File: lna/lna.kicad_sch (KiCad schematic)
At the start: 12 parts, among them J1 Conn_Coaxial, J2 V5-GND, U1 PGA-103+

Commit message: Schematics
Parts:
- removed C3: 0.01uF, symbol Device:C
- added C?: 0.33uF, symbol Device:C
- added C?: 10uF, symbol Device:CP1
- added J?: Conn_Coaxial, symbol Connector:Conn_Coaxial
- added L?: 220nH, symbol Device:L
- added L?: 310nH, symbol Device:L
- L3: value 620nH -> 310nH
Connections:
- net 5V: now also C?.1, C?.1, L?.2
- net GND: now also J1.2 (Ext), C?.2, C?.2, J?.2 (Ext); no longer J1.1 (In)
- net at C1.1, C2.1, L1.1: now also J1.1 (In); no longer J1.2 (Ext)
- net at R1.1: now also L?.2; no longer L3.2
- net at L2.2: now also L3.1, U1.1
- net at C5.1, U1.3: now also L?.1
- net at C5.2: now also J?.1 (In)
- new net: L3.2, L?.1
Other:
- moved on the sheet: C1, C2, C4, C5, J1, J2, L1, L2, L3, R1, U1

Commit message: Footprints
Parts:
- C1, C2: footprint (none) -> Capacitor_SMD:C_0603_1608Metric
- C3: renamed from C4; footprint (none) -> Capacitor_SMD:C_0603_1608Metric
- C4: renamed from C?; footprint (none) -> Capacitor_SMD:C_0603_1608Metric
- C5: renamed from C?; footprint (none) -> Capacitor_Tantalum_SMD:CP_EIA-3216-18_Kemet-A
- C6: renamed from C5; footprint (none) -> Capacitor_SMD:C_0603_1608Metric
- J1: footprint (none) -> Connector_Coaxial:SMA_Amphenol_132289_EdgeMount
- J2: footprint (none) -> Connector_PinHeader_2.54mm:PinHeader_1x02_P2.54mm_Vertical
- J3: renamed from J?; footprint (none) -> Connector_Coaxial:SMA_Amphenol_132203-12_Horizontal
- L1, L2, L3: footprint (none) -> Inductor_SMD:L_0805_2012Metric
- L4, L5: renamed from L?; footprint (none) -> Inductor_SMD:L_0805_2012Metric
- R1: footprint (none) -> Resistor_SMD:R_0603_1608Metric

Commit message: PCB part 1
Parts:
- J3: footprint Connector_Coaxial:SMA_Amphenol_132203-12_Horizontal -> Connector_Coaxial:SMA_Amphenol_132289_EdgeMount
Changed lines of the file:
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@@
     (property "Reference" "J3" (id 0) (at 179.9782 33.5153 0))
     (property "Value" "Conn_Coaxial" (id 1) (at 180.2195 36.0553 0))
-    (property "Footprint" "Connector_Coaxial:SMA_Amphenol_132203-12_Horizontal" (id 2) (at 180.34 40.64 0)
+    (property "Footprint" "Connector_Coaxial:SMA_Amphenol_132289_EdgeMount" (id 2) (at 180.34 40.64 0)
       (effects (font (size 1.27 1.27)) hide)
     )
@@
     )
     (path "/7cd1b49d-2904-4036-9173-3a8bf4b4b229"
-      (reference "J3") (unit 1) (value "Conn_Coaxial") (footprint "Connector_Coaxial:SMA_Amphenol_132203-12_Horizontal")
+      (reference "J3") (unit 1) (value "Conn_Coaxial") (footprint "Connector_Coaxial:SMA_Amphenol_132289_EdgeMount")
     )
     (path "/5c96d87d-8e59-4bd2-bdb2-f94bde9c9bde"

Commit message: Routes
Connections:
- net at C2.2: now also L2.2; no longer L2.1
- net at L3.1, U1.1: now also L2.1; no longer L2.2
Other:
- moved on the sheet: L2
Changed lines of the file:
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@@
     )
   )
-  (symbol (lib_id "Device:L") (at 85.09 40.64 90) (unit 1)
+  (symbol (lib_id "Device:L") (at 85.09 40.64 270) (unit 1)
     (in_bom yes) (on_board yes)
-    (property "Reference" "L2" (id 0) (at 86.4806 35.5599 90)
+    (property "Reference" "L2" (id 0) (at 83.6994 45.7201 90)
       (effects (font (size 1.27 1.27)) (justify left))
     )
-    (property "Value" "120nH" (id 1) (at 84.969 38.1 90))
+    (property "Value" "120nH" (id 1) (at 85.211 43.18 90))
     (property "Footprint" "Inductor_SMD:L_0805_2012Metric" (id 2) (at 85.09 40.64 0)
       (effects (font (size 1.27 1.27)) hide)

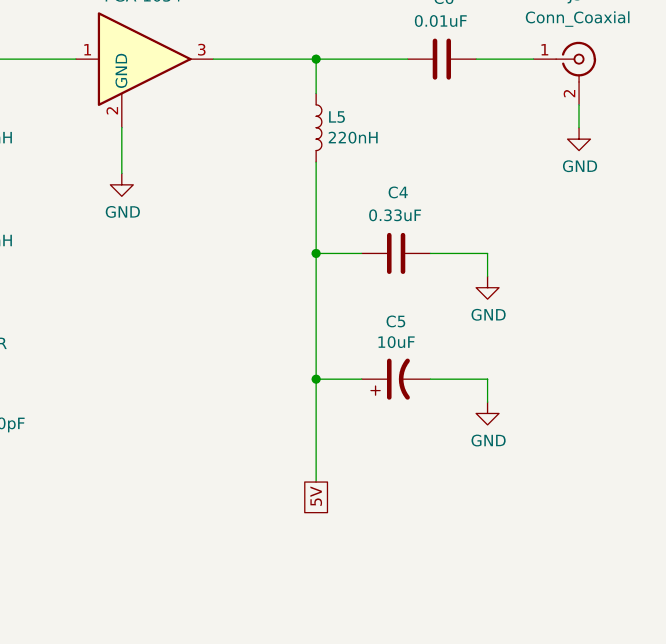
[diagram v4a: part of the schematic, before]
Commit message: Add ferrite bead
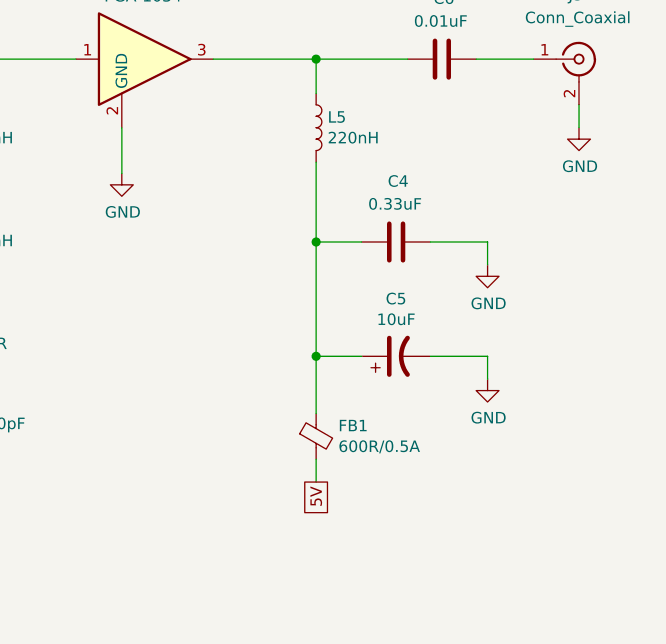
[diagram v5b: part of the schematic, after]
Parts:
- added FB1: 600R/0.5A, fbead:Murata-BLM18-0.15-t0.8-0-0-IPC_A, symbol Device:Ferrite_Bead_Small
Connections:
- net 5V: now also FB1.2; no longer C4.1, C5.1, L5.2
- new net: C4.1, C5.1, FB1.1, L5.2
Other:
- moved on the sheet: C4, C5
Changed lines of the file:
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@@
   (junction (at 110.49 40.64) (diameter 1.016) (color 0 0 0 0))
   (junction (at 151.13 40.64) (diameter 1.016) (color 0 0 0 0))
-  (junction (at 151.13 62.23) (diameter 1.016) (color 0 0 0 0))
-  (junction (at 151.13 76.2) (diameter 1.016) (color 0 0 0 0))
+  (junction (at 151.13 60.96) (diameter 1.016) (color 0 0 0 0))
+  (junction (at 151.13 73.66) (diameter 1.016) (color 0 0 0 0))
   (wire (pts (xy 29.21 45.72) (xy 29.21 48.26))
     (stroke (width 0) (type solid) (color 0 0 0 0))
@@
     (stroke (width 0) (type solid) (color 0 0 0 0))
   )
-  (wire (pts (xy 151.13 52.07) (xy 151.13 62.23))
-    (stroke (width 0) (type solid) (color 0 0 0 0))
-  )
-  (wire (pts (xy 151.13 62.23) (xy 151.13 76.2))
-    (stroke (width 0) (type solid) (color 0 0 0 0))
-  )
-  (wire (pts (xy 151.13 62.23) (xy 156.21 62.23))
-    (stroke (width 0) (type solid) (color 0 0 0 0))
-  )
-  (wire (pts (xy 151.13 76.2) (xy 151.13 87.63))
-    (stroke (width 0) (type solid) (color 0 0 0 0))
-  )
-  (wire (pts (xy 151.13 76.2) (xy 156.21 76.2))
-    (stroke (width 0) (type solid) (color 0 0 0 0))
-  )
-  (wire (pts (xy 163.83 62.23) (xy 170.18 62.23))
-    (stroke (width 0) (type solid) (color 0 0 0 0))
-  )
-  (wire (pts (xy 163.83 76.2) (xy 170.18 76.2))
+  (wire (pts (xy 151.13 52.07) (xy 151.13 60.96))
+    (stroke (width 0) (type solid) (color 0 0 0 0))
+  )
+  (wire (pts (xy 151.13 60.96) (xy 151.13 73.66))
+    (stroke (width 0) (type solid) (color 0 0 0 0))
+  )
+  (wire (pts (xy 151.13 60.96) (xy 156.21 60.96))
+    (stroke (width 0) (type solid) (color 0 0 0 0))
+  )
+  (wire (pts (xy 151.13 73.66) (xy 151.13 80.01))
+    (stroke (width 0) (type solid) (color 0 0 0 0))
+  )
+  (wire (pts (xy 151.13 73.66) (xy 156.21 73.66))
+    (stroke (width 0) (type solid) (color 0 0 0 0))
+  )
+  (wire (pts (xy 151.13 85.09) (xy 151.13 87.63))
+    (stroke (width 0) (type solid) (color 0 0 0 0))
+  )
+  (wire (pts (xy 163.83 60.96) (xy 170.18 60.96))
+    (stroke (width 0) (type solid) (color 0 0 0 0))
+  )
+  (wire (pts (xy 163.83 73.66) (xy 170.18 73.66))
     (stroke (width 0) (type solid) (color 0 0 0 0))
   )
@@
     (stroke (width 0) (type solid) (color 0 0 0 0))
   )
-  (wire (pts (xy 170.18 64.77) (xy 170.18 62.23))
-    (stroke (width 0) (type solid) (color 0 0 0 0))
-  )
-  (wire (pts (xy 170.18 76.2) (xy 170.18 78.74))
+  (wire (pts (xy 170.18 63.5) (xy 170.18 60.96))
+    (stroke (width 0) (type solid) (color 0 0 0 0))
+  )
+  (wire (pts (xy 170.18 73.66) (xy 170.18 76.2))
     (stroke (width 0) (type solid) (color 0 0 0 0))
   )
@@
     )
   )
-  (symbol (lib_id "power:GND") (at 170.18 64.77 0) (unit 1)
-    (in_bom yes) (on_board yes)
-    (property "Reference" "#PWR07" (id 0) (at 170.18 71.12 0)
-      (effects (font (size 1.27 1.27)) hide)
-    )
-    (property "Value" "GND" (id 1) (at 170.2943 69.0944 0))
-    (property "Footprint" "" (id 2) (at 170.18 64.77 0)
-      (effects (font (size 1.27 1.27)) hide)
-    )
-    (property "Datasheet" "" (id 3) (at 170.18 64.77 0)
-      (effects (font (size 1.27 1.27)) hide)
-    )
-  )
-  (symbol (lib_id "power:GND") (at 170.18 78.74 0) (unit 1)
-    (in_bom yes) (on_board yes)
-    (property "Reference" "#PWR08" (id 0) (at 170.18 85.09 0)
-      (effects (font (size 1.27 1.27)) hide)
-    )
-    (property "Value" "GND" (id 1) (at 170.2943 83.0644 0))
-    (property "Footprint" "" (id 2) (at 170.18 78.74 0)
-      (effects (font (size 1.27 1.27)) hide)
-    )
-    (property "Datasheet" "" (id 3) (at 170.18 78.74 0)
+  (symbol (lib_id "power:GND") (at 170.18 63.5 0) (unit 1)
+    (in_bom yes) (on_board yes)
+    (property "Reference" "#PWR07" (id 0) (at 170.18 69.85 0)
+      (effects (font (size 1.27 1.27)) hide)
+    )
+    (property "Value" "GND" (id 1) (at 170.2943 67.8244 0))
+    (property "Footprint" "" (id 2) (at 170.18 63.5 0)
+      (effects (font (size 1.27 1.27)) hide)
+    )
+    (property "Datasheet" "" (id 3) (at 170.18 63.5 0)
+      (effects (font (size 1.27 1.27)) hide)
+    )
+  )
+  (symbol (lib_id "power:GND") (at 170.18 76.2 0) (unit 1)
+    (in_bom yes) (on_board yes)
+    (property "Reference" "#PWR08" (id 0) (at 170.18 82.55 0)
+      (effects (font (size 1.27 1.27)) hide)
+    )
+    (property "Value" "GND" (id 1) (at 170.2943 80.5244 0))
+    (property "Footprint" "" (id 2) (at 170.18 76.2 0)
+      (effects (font (size 1.27 1.27)) hide)
+    )
+    (property "Datasheet" "" (id 3) (at 170.18 76.2 0)
       (effects (font (size 1.27 1.27)) hide)
     )
@@
     )
   )
+  (symbol (lib_id "Device:Ferrite_Bead_Small") (at 151.13 82.55 0) (unit 1)
+    (in_bom yes) (on_board yes)
+    (property "Reference" "FB1" (id 0) (at 153.5939 81.4006 0)
+      (effects (font (size 1.27 1.27)) (justify left))
+    )
+    (property "Value" "600R/0.5A" (id 1) (at 153.594 83.699 0)
+      (effects (font (size 1.27 1.27)) (justify left))
+    )
+    (property "Footprint" "fbead:Murata-BLM18-0.15-t0.8-0-0-IPC_A" (id 2) (at 149.352 82.55 90)
+      (effects (font (size 1.27 1.27)) hide)
+    )
+    (property "Datasheet" "~" (id 3) (at 151.13 82.55 0)
+      (effects (font (size 1.27 1.27)) hide)
+    )
+  )
   (symbol (lib_id "Device:C") (at 52.07 46.99 0) (unit 1)
     (in_bom yes) (on_board yes)
@@
     )
   )
-  (symbol (lib_id "Device:C") (at 160.02 62.23 90) (unit 1)
-    (in_bom yes) (on_board yes)
-    (property "Reference" "C4" (id 0) (at 161.4106 55.4989 90)
-      (effects (font (size 1.27 1.27)) (justify left))
-    )
-    (property "Value" "0.33uF" (id 1) (at 159.899 58.039 90))
-    (property "Footprint" "Capacitor_SMD:C_0603_1608Metric" (id 2) (at 163.83 61.2648 0)
-      (effects (font (size 1.27 1.27)) hide)
-    )
-    (property "Datasheet" "~" (id 3) (at 160.02 62.23 0)
-      (effects (font (size 1.27 1.27)) hide)
-    )
-  )
-  (symbol (lib_id "Device:CP1") (at 160.02 76.2 90) (unit 1)
-    (in_bom yes) (on_board yes)
-    (property "Reference" "C5" (id 0) (at 160.02 69.8308 90))
-    (property "Value" "10uF" (id 1) (at 160.02 72.13 90))
-    (property "Footprint" "Capacitor_Tantalum_SMD:CP_EIA-3216-18_Kemet-A" (id 2) (at 160.02 76.2 0)
-      (effects (font (size 1.27 1.27)) hide)
-    )
-    (property "Datasheet" "~" (id 3) (at 160.02 76.2 0)
+  (symbol (lib_id "Device:C") (at 160.02 60.96 90) (unit 1)
+    (in_bom yes) (on_board yes)
+    (property "Reference" "C4" (id 0) (at 161.4106 54.2289 90)
+      (effects (font (size 1.27 1.27)) (justify left))
+    )
+    (property "Value" "0.33uF" (id 1) (at 159.899 56.769 90))
+    (property "Footprint" "Capacitor_SMD:C_0603_1608Metric" (id 2) (at 163.83 59.9948 0)
+      (effects (font (size 1.27 1.27)) hide)
+    )
+    (property "Datasheet" "~" (id 3) (at 160.02 60.96 0)
+      (effects (font (size 1.27 1.27)) hide)
+    )
+  )
+  (symbol (lib_id "Device:CP1") (at 160.02 73.66 90) (unit 1)
+    (in_bom yes) (on_board yes)
+    (property "Reference" "C5" (id 0) (at 160.02 67.2908 90))
+    (property "Value" "10uF" (id 1) (at 160.02 69.59 90))
+    (property "Footprint" "Capacitor_Tantalum_SMD:CP_EIA-3216-18_Kemet-A" (id 2) (at 160.02 73.66 0)
+      (effects (font (size 1.27 1.27)) hide)
+    )
+    (property "Datasheet" "~" (id 3) (at 160.02 73.66 0)
       (effects (font (size 1.27 1.27)) hide)
     )
@@
       (reference "C6") (unit 1) (value "0.01uF") (footprint "Capacitor_SMD:C_0603_1608Metric")
     )
+    (path "/05f9fadf-aa2f-47ef-81aa-f9fd3cd4830a"
+      (reference "FB1") (unit 1) (value "600R/0.5A") (footprint "fbead:Murata-BLM18-0.15-t0.8-0-0-IPC_A")
+    )
     (path "/30b0c4e7-8b2a-4a6c-8198-8d23d0eeeb5e"

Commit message: Final v1
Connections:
- net 5V: now also FB1.1; no longer FB1.2
- net at C4.1, C5.1, L5.2: now also FB1.2; no longer FB1.1
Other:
- moved on the sheet: FB1
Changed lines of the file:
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@@
     )
   )
-  (symbol (lib_id "Device:Ferrite_Bead_Small") (at 151.13 82.55 0) (unit 1)
+  (symbol (lib_id "Device:Ferrite_Bead_Small") (at 151.13 82.55 180) (unit 1)
     (in_bom yes) (on_board yes)
-    (property "Reference" "FB1" (id 0) (at 153.5939 81.4006 0)
+    (property "Reference" "FB1" (id 0) (at 148.6661 83.6994 0)
       (effects (font (size 1.27 1.27)) (justify left))
     )
-    (property "Value" "600R/0.5A" (id 1) (at 153.594 83.699 0)
+    (property "Value" "600R/0.5A" (id 1) (at 148.666 81.401 0)
       (effects (font (size 1.27 1.27)) (justify left))
     )
-    (property "Footprint" "fbead:Murata-BLM18-0.15-t0.8-0-0-IPC_A" (id 2) (at 149.352 82.55 90)
+    (property "Footprint" "fbead:Murata-BLM18-0.15-t0.8-0-0-IPC_A" (id 2) (at 152.908 82.55 90)
       (effects (font (size 1.27 1.27)) hide)
     )

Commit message: Add some fixes
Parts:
- added C4: 100pF, Capacitor_SMD:C_0603_1608Metric, symbol Device:C
- C5: renamed from C4; value 0.33uF -> 100nF
- C7: renamed from C6; value 0.01uF -> 100pF
- renumbered C5 to C6
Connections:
- net GND: now also C4.1
- net at C5.1, C6.1, FB1.2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: now also C4.2
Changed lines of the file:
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@@
   (junction (at 151.13 40.64) (diameter 1.016) (color 0 0 0 0))
   (junction (at 151.13 60.96) (diameter 1.016) (color 0 0 0 0))
+  (junction (at 151.13 67.31) (diameter 1.016) (color 0 0 0 0))
   (junction (at 151.13 73.66) (diameter 1.016) (color 0 0 0 0))
   (wire (pts (xy 29.21 45.72) (xy 29.21 48.26))
@@
     (stroke (width 0) (type solid) (color 0 0 0 0))
   )
+  (wire (pts (xy 132.08 67.31) (xy 132.08 69.85))
+    (stroke (width 0) (type solid) (color 0 0 0 0))
+  )
+  (wire (pts (xy 132.08 67.31) (xy 137.16 67.31))
+    (stroke (width 0) (type solid) (color 0 0 0 0))
+  )
   (wire (pts (xy 139.7 40.64) (xy 151.13 40.64))
     (stroke (width 0) (type solid) (color 0 0 0 0))
   )
+  (wire (pts (xy 144.78 67.31) (xy 151.13 67.31))
+    (stroke (width 0) (type solid) (color 0 0 0 0))
+  )
   (wire (pts (xy 151.13 40.64) (xy 151.13 44.45))
     (stroke (width 0) (type solid) (color 0 0 0 0))
@@
     (stroke (width 0) (type solid) (color 0 0 0 0))
   )
-  (wire (pts (xy 151.13 60.96) (xy 151.13 73.66))
+  (wire (pts (xy 151.13 60.96) (xy 151.13 67.31))
     (stroke (width 0) (type solid) (color 0 0 0 0))
   )
   (wire (pts (xy 151.13 60.96) (xy 156.21 60.96))
+    (stroke (width 0) (type solid) (color 0 0 0 0))
+  )
+  (wire (pts (xy 151.13 67.31) (xy 151.13 73.66))
     (stroke (width 0) (type solid) (color 0 0 0 0))
   )
@@
     )
   )
+  (symbol (lib_id "power:GND") (at 132.08 69.85 0) (unit 1)
+    (in_bom yes) (on_board yes)
+    (property "Reference" "#PWR07" (id 0) (at 132.08 76.2 0)
+      (effects (font (size 1.27 1.27)) hide)
+    )
+    (property "Value" "GND" (id 1) (at 132.1943 74.1744 0))
+    (property "Footprint" "" (id 2) (at 132.08 69.85 0)
+      (effects (font (size 1.27 1.27)) hide)
+    )
+    (property "Datasheet" "" (id 3) (at 132.08 69.85 0)
+      (effects (font (size 1.27 1.27)) hide)
+    )
+  )
   (symbol (lib_id "power:GND") (at 170.18 63.5 0) (unit 1)
     (in_bom yes) (on_board yes)
-    (property "Reference" "#PWR07" (id 0) (at 170.18 69.85 0)
+    (property "Reference" "#PWR08" (id 0) (at 170.18 69.85 0)
       (effects (font (size 1.27 1.27)) hide)
     )
@@
   (symbol (lib_id "power:GND") (at 170.18 76.2 0) (unit 1)
     (in_bom yes) (on_board yes)
-    (property "Reference" "#PWR08" (id 0) (at 170.18 82.55 0)
+    (property "Reference" "#PWR09" (id 0) (at 170.18 82.55 0)
       (effects (font (size 1.27 1.27)) hide)
     )
@@
   (symbol (lib_id "power:GND") (at 180.34 48.26 0) (unit 1)
     (in_bom yes) (on_board yes)
-    (property "Reference" "#PWR09" (id 0) (at 180.34 54.61 0)
+    (property "Reference" "#PWR010" (id 0) (at 180.34 54.61 0)
       (effects (font (size 1.27 1.27)) hide)
     )
@@
     )
   )
+  (symbol (lib_id "Device:C") (at 140.97 67.31 90) (unit 1)
+    (in_bom yes) (on_board yes)
+    (property "Reference" "C4" (id 0) (at 142.3606 60.5789 90)
+      (effects (font (size 1.27 1.27)) (justify left))
+    )
+    (property "Value" "100pF" (id 1) (at 140.849 63.119 90))
+    (property "Footprint" "Capacitor_SMD:C_0603_1608Metric" (id 2) (at 144.78 66.3448 0)
+      (effects (font (size 1.27 1.27)) hide)
+    )
+    (property "Datasheet" "~" (id 3) (at 140.97 67.31 0)
+      (effects (font (size 1.27 1.27)) hide)
+    )
+  )
   (symbol (lib_id "Device:C") (at 160.02 60.96 90) (unit 1)
     (in_bom yes) (on_board yes)
-    (property "Reference" "C4" (id 0) (at 161.4106 54.2289 90)
-      (effects (font (size 1.27 1.27)) (justify left))
-    )
-    (property "Value" "0.33uF" (id 1) (at 159.899 56.769 90))
+    (property "Reference" "C5" (id 0) (at 161.4106 54.2289 90)
+      (effects (font (size 1.27 1.27)) (justify left))
+    )
+    (property "Value" "100nF" (id 1) (at 159.899 56.769 90))
     (property "Footprint" "Capacitor_SMD:C_0603_1608Metric" (id 2) (at 163.83 59.9948 0)
       (effects (font (size 1.27 1.27)) hide)
@@
   (symbol (lib_id "Device:CP1") (at 160.02 73.66 90) (unit 1)
     (in_bom yes) (on_board yes)
-    (property "Reference" "C5" (id 0) (at 160.02 67.2908 90))
+    (property "Reference" "C6" (id 0) (at 160.02 67.2908 90))
     (property "Value" "10uF" (id 1) (at 160.02 69.59 90))
     (property "Footprint" "Capacitor_Tantalum_SMD:CP_EIA-3216-18_Kemet-A" (id 2) (at 160.02 73.66 0)
@@
   (symbol (lib_id "Device:C") (at 165.1 40.64 90) (unit 1)
     (in_bom yes) (on_board yes)
-    (property "Reference" "C6" (id 0) (at 166.4906 33.9089 90)
-      (effects (font (size 1.27 1.27)) (justify left))
-    )
-    (property "Value" "0.01uF" (id 1) (at 164.979 36.449 90))
+    (property "Reference" "C7" (id 0) (at 166.4906 33.9089 90)
+      (effects (font (size 1.27 1.27)) (justify left))
+    )
+    (property "Value" "100pF" (id 1) (at 164.979 36.449 90))
     (property "Footprint" "Capacitor_SMD:C_0603_1608Metric" (id 2) (at 168.91 39.6748 0)
       (effects (font (size 1.27 1.27)) hide)
@@
       (reference "#PWR06") (unit 1) (value "GND") (footprint "")
     )
+    (path "/af03b1ac-a63e-4589-9bd3-6c4073ddcf18"
+      (reference "#PWR07") (unit 1) (value "GND") (footprint "")
+    )
     (path "/38163c67-0a1e-466f-ba31-fca0bc0a0ca3"
-      (reference "#PWR07") (unit 1) (value "GND") (footprint "")
+      (reference "#PWR08") (unit 1) (value "GND") (footprint "")
     )
     (path "/8a06f8df-9ccd-403b-a4ab-8fe870fccfc9"
-      (reference "#PWR08") (unit 1) (value "GND") (footprint "")
+      (reference "#PWR09") (unit 1) (value "GND") (footprint "")
     )
     (path "/64c4a37b-56b7-4b33-a7cc-7480bced206c"
-      (reference "#PWR09") (unit 1) (value "GND") (footprint "")
+      (reference "#PWR010") (unit 1) (value "GND") (footprint "")
     )
     (path "/e3613cca-fb62-4c1e-9e92-3c0f2f895470"
@@
       (reference "C3") (unit 1) (value "330pF") (footprint "Capacitor_SMD:C_0603_1608Metric")
     )
+    (path "/3a0f0ae0-a5fe-4280-b3bf-507e9bd2aeef"
+      (reference "C4") (unit 1) (value "100pF") (footprint "Capacitor_SMD:C_0603_1608Metric")
+    )
     (path "/0ee982c6-69e7-4b82-bafe-c5d5a95c9df6"
-      (reference "C4") (unit 1) (value "0.33uF") (footprint "Capacitor_SMD:C_0603_1608Metric")
+      (reference "C5") (unit 1) (value "100nF") (footprint "Capacitor_SMD:C_0603_1608Metric")
     )
     (path "/8b0f5856-894b-4361-a691-0dfceff3d838"
-      (reference "C5") (unit 1) (value "10uF") (footprint "Capacitor_Tantalum_SMD:CP_EIA-3216-18_Kemet-A")
+      (reference "C6") (unit 1) (value "10uF") (footprint "Capacitor_Tantalum_SMD:CP_EIA-3216-18_Kemet-A")
     )
     (path "/954c8f38-a277-4649-9bd1-91c1a696d3ab"
-      (reference "C6") (unit 1) (value "0.01uF") (footprint "Capacitor_SMD:C_0603_1608Metric")
+      (reference "C7") (unit 1) (value "100pF") (footprint "Capacitor_SMD:C_0603_1608Metric")
     )
     (path "/05f9fadf-aa2f-47ef-81aa-f9fd3cd4830a"
